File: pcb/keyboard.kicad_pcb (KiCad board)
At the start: 4 copper layers, 141 x 99 mm, 29 parts

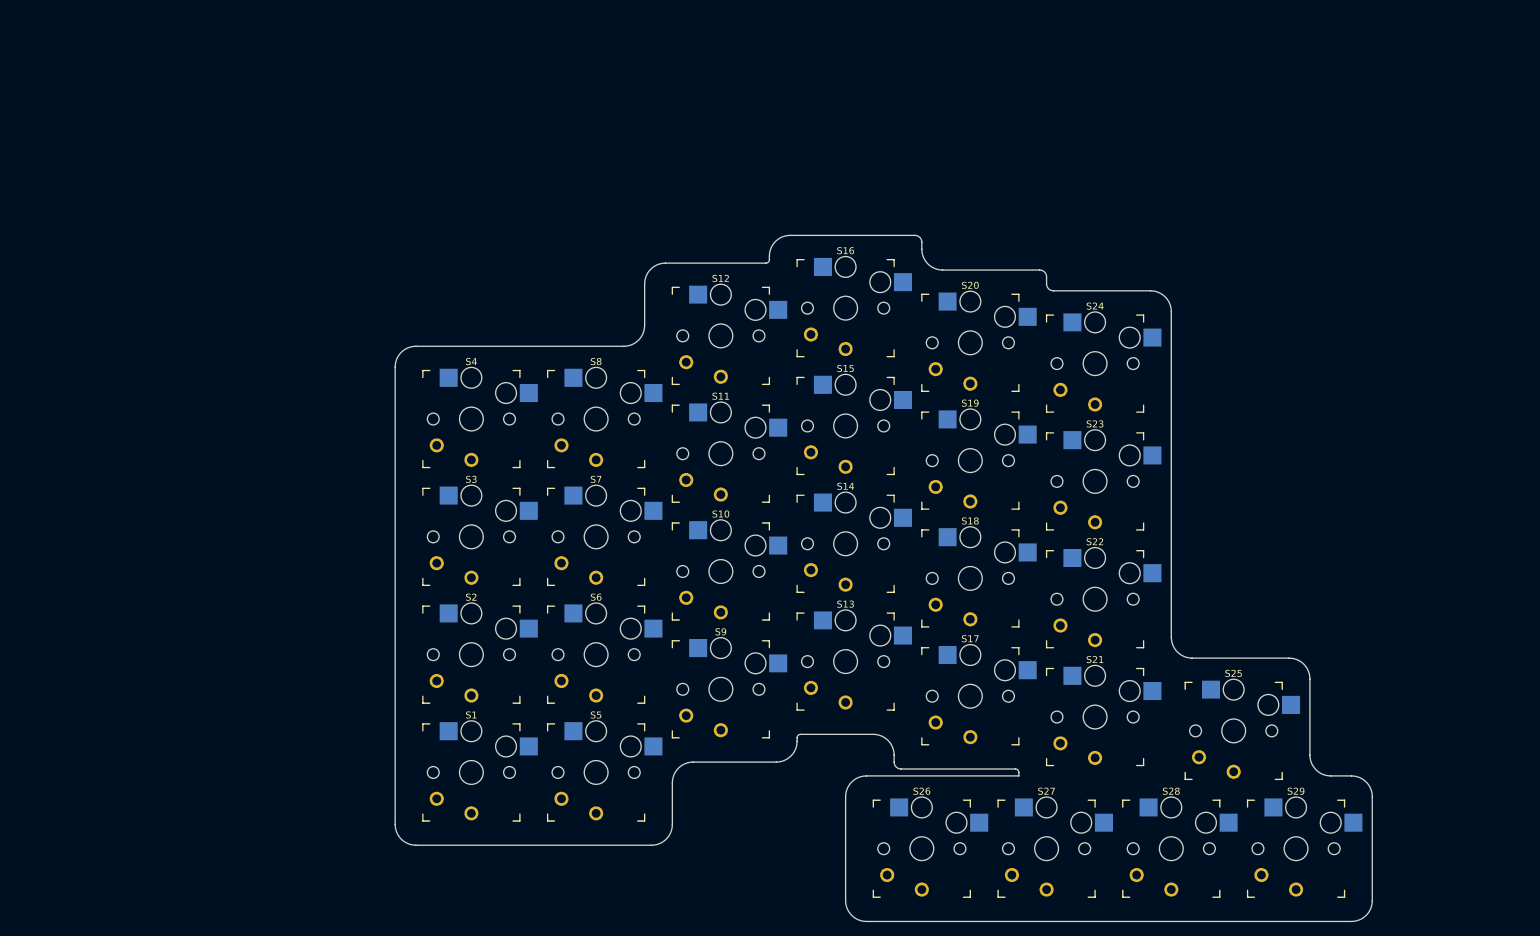
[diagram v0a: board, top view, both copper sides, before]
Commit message: #2 Import schematic components to the PCB
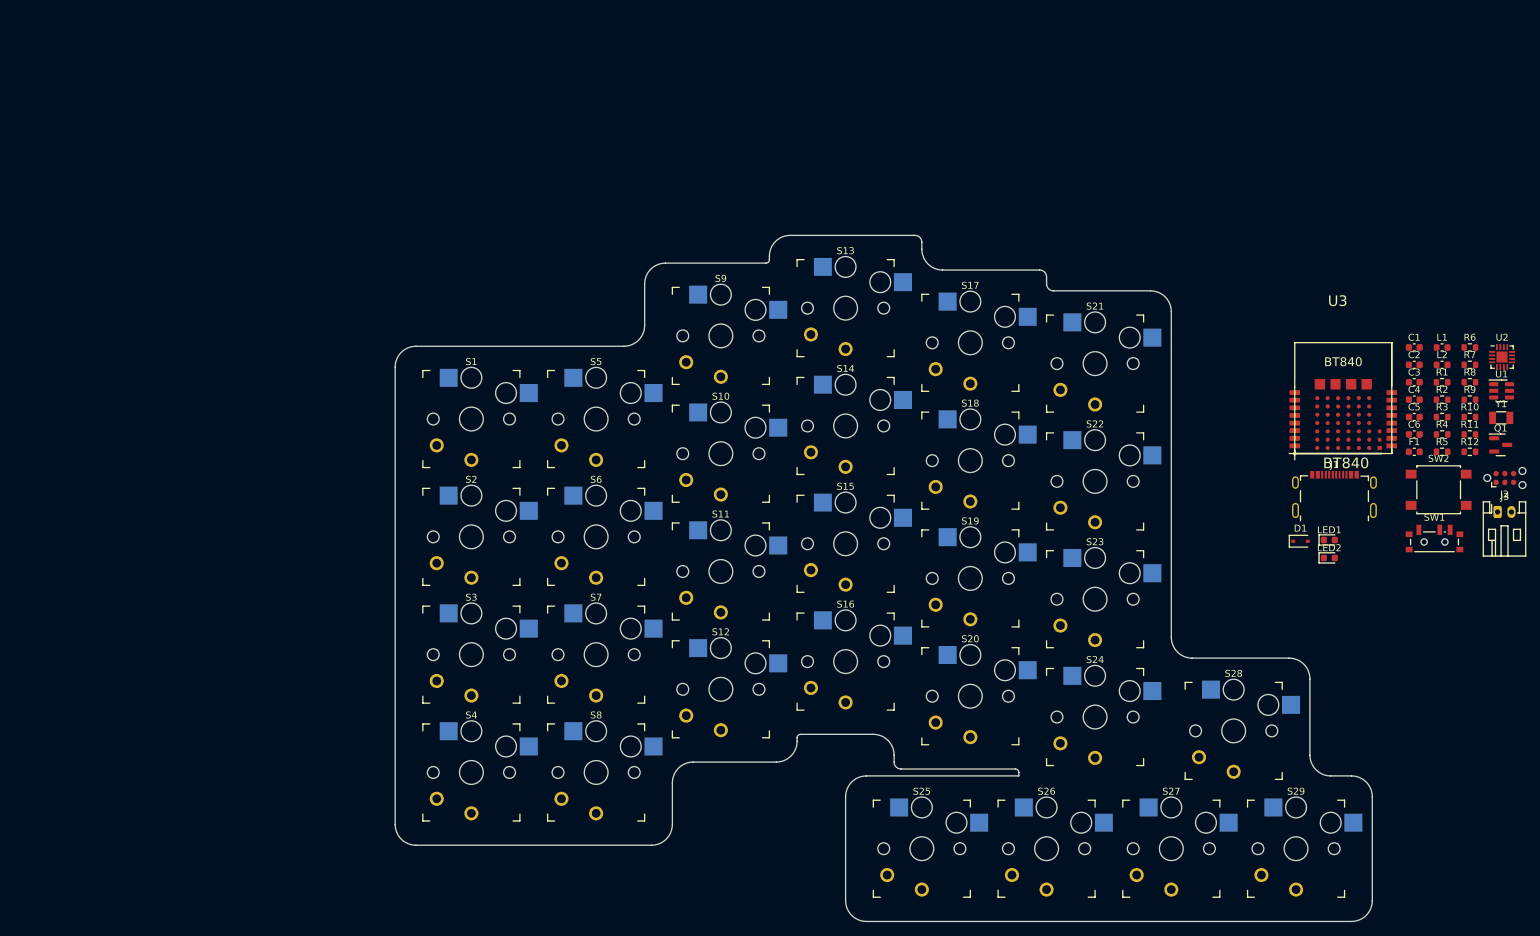
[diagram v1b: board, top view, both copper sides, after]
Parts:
- added C1: 100 nF, Capacitor_SMD:C_0603_1608Metric, F.Cu at (280.2, 88.5)
- added C2: 4.7 uF, Capacitor_SMD:C_0603_1608Metric, F.Cu at (280.2, 91.0)
- added C3: 4.7 uF, Capacitor_SMD:C_0603_1608Metric, F.Cu at (280.2, 93.5)
- added C4: 4.7 uF, Capacitor_SMD:C_0603_1608Metric, F.Cu at (280.2, 96.0)
- added C5: 12pF, Capacitor_SMD:C_0603_1608Metric, F.Cu at (280.2, 98.5)
- added C6: 12pF, Capacitor_SMD:C_0603_1608Metric, F.Cu at (280.2, 101.1)
- added D1: STS321050B100, Diode_SMD:D_SOD-323, F.Cu at (263.8, 116.5)
- added F1: ERB-RE0R75V, Fuse:Fuse_0603_1608Metric, F.Cu at (280.2, 103.6)
- added J1: USB4510-03-1-A, keyboard:USB_C_Receptacle_GCT_USB4510-03-1-A, F.Cu at (268.7, 111.1)
- added J2: Battery, Connector_JST:JST_PH_S2B-PH-K_1x02_P2.00mm_Horizontal, F.Cu at (292.2, 112.2)
- added J3: Tag-Connect TC2030, Connector:Tag-Connect_TC2030-IDC-NL_2x03_P1.27mm_Vertical, F.Cu at (293.2, 107.3)
- added L1: BLM18SG121TN1D, Inductor_SMD:L_0603_1608Metric, F.Cu at (284.2, 88.5)
- added L2: BLM18SG121TN1D, Inductor_SMD:L_0603_1608Metric, F.Cu at (284.2, 91.0)
- added LED1: orange, LED_SMD:LED_0603_1608Metric, F.Cu at (267.9, 116.3)
- added LED2: green, LED_SMD:LED_0603_1608Metric, F.Cu at (267.9, 118.9)
- added Q1: 2N7002, Package_TO_SOT_SMD:SOT-23, F.Cu at (292.6, 102.6)
- added R1: 1 MOhm, Resistor_SMD:R_0603_1608Metric, F.Cu at (284.2, 93.5)
- added R10: 10 kOhm, Resistor_SMD:R_0603_1608Metric, F.Cu at (288.2, 98.5)
- added R11: 100 kOhm, Resistor_SMD:R_0603_1608Metric, F.Cu at (288.2, 101.1)
- added R12: 470 Ohm, Resistor_SMD:R_0603_1608Metric, F.Cu at (288.2, 103.6)
- added R2: 5.1 kOhm, Resistor_SMD:R_0603_1608Metric, F.Cu at (284.2, 96.0)
- added R3: 5.1 kOhm, Resistor_SMD:R_0603_1608Metric, F.Cu at (284.2, 98.5)
- added R4: 47 kOhm, Resistor_SMD:R_0603_1608Metric, F.Cu at (284.2, 101.1)
- added R5: 1.5 kOhm, Resistor_SMD:R_0603_1608Metric, F.Cu at (284.2, 103.6)
- added R6: 5.6 kOhm, Resistor_SMD:R_0603_1608Metric, F.Cu at (288.2, 88.5)
- added R7: 10 kOhm, Resistor_SMD:R_0603_1608Metric, F.Cu at (288.2, 91.0)
- added R8: 1.5 kOhm, Resistor_SMD:R_0603_1608Metric, F.Cu at (288.2, 93.5)
- added R9: 100 Ohm, Resistor_SMD:R_0603_1608Metric, F.Cu at (288.2, 96.0)
- added SW1: PWR, keyboard:SW_SPDT_PCM12, F.Cu at (283.1, 116.2)
- added SW2: Reset, Button_Switch_SMD:SW_SPST_B3S-1000, F.Cu at (283.7, 109.0)
- added U1: SRV05-4, Package_TO_SOT_SMD:SOT-23-6, F.Cu at (292.8, 94.8)
- added U2: BQ24075, Package_DFN_QFN:VQFN-16-1EP_3x3mm_P0.5mm_EP1.6x1.6mm, F.Cu at (292.9, 89.9)
- added U3: BT840, keyboard:Fanstel_BT840, F.Cu at (262.9, 103.8)
- added Y1: ECS-.327-9-34B-TR, Crystal:Crystal_SMD_3215-2Pin_3.2x1.5mm, F.Cu at (292.7, 98.7)
- S1: renamed from S4; footprint kali_choc_v1:Kailh_socket_PG1350_optional -> keyboard:Kailh_socket_PG1350_optional
- S10: renamed from S11; footprint kali_choc_v1:Kailh_socket_PG1350_optional -> keyboard:Kailh_socket_PG1350_optional
- S11: renamed from S10; footprint kali_choc_v1:Kailh_socket_PG1350_optional -> keyboard:Kailh_socket_PG1350_optional
- S12: renamed from S9; footprint kali_choc_v1:Kailh_socket_PG1350_optional -> keyboard:Kailh_socket_PG1350_optional
- S13: renamed from S16; footprint kali_choc_v1:Kailh_socket_PG1350_optional -> keyboard:Kailh_socket_PG1350_optional
- S14: renamed from S15; footprint kali_choc_v1:Kailh_socket_PG1350_optional -> keyboard:Kailh_socket_PG1350_optional
- S15: renamed from S14; footprint kali_choc_v1:Kailh_socket_PG1350_optional -> keyboard:Kailh_socket_PG1350_optional
- S16: renamed from S13; footprint kali_choc_v1:Kailh_socket_PG1350_optional -> keyboard:Kailh_socket_PG1350_optional
- S17: renamed from S20; footprint kali_choc_v1:Kailh_socket_PG1350_optional -> keyboard:Kailh_socket_PG1350_optional
- S18: renamed from S19; footprint kali_choc_v1:Kailh_socket_PG1350_optional -> keyboard:Kailh_socket_PG1350_optional
- S19: renamed from S18; footprint kali_choc_v1:Kailh_socket_PG1350_optional -> keyboard:Kailh_socket_PG1350_optional
- S2: renamed from S3; footprint kali_choc_v1:Kailh_socket_PG1350_optional -> keyboard:Kailh_socket_PG1350_optional
- S20: renamed from S17; footprint kali_choc_v1:Kailh_socket_PG1350_optional -> keyboard:Kailh_socket_PG1350_optional
- S21: renamed from S24; footprint kali_choc_v1:Kailh_socket_PG1350_optional -> keyboard:Kailh_socket_PG1350_optional
- S22: renamed from S23; footprint kali_choc_v1:Kailh_socket_PG1350_optional -> keyboard:Kailh_socket_PG1350_optional
- S23: renamed from S22; footprint kali_choc_v1:Kailh_socket_PG1350_optional -> keyboard:Kailh_socket_PG1350_optional
- S24: renamed from S21; footprint kali_choc_v1:Kailh_socket_PG1350_optional -> keyboard:Kailh_socket_PG1350_optional
- S25: renamed from S26; footprint kali_choc_v1:Kailh_socket_PG1350_optional -> keyboard:Kailh_socket_PG1350_optional
- S26: renamed from S27; footprint kali_choc_v1:Kailh_socket_PG1350_optional -> keyboard:Kailh_socket_PG1350_optional
- S27: renamed from S28; footprint kali_choc_v1:Kailh_socket_PG1350_optional -> keyboard:Kailh_socket_PG1350_optional
- S28: renamed from S25; footprint kali_choc_v1:Kailh_socket_PG1350_optional -> keyboard:Kailh_socket_PG1350_optional
- S29: footprint kali_choc_v1:Kailh_socket_PG1350_optional -> keyboard:Kailh_socket_PG1350_optional
- S3: renamed from S2; footprint kali_choc_v1:Kailh_socket_PG1350_optional -> keyboard:Kailh_socket_PG1350_optional
- S4: renamed from S1; footprint kali_choc_v1:Kailh_socket_PG1350_optional -> keyboard:Kailh_socket_PG1350_optional
- S5: renamed from S8; footprint kali_choc_v1:Kailh_socket_PG1350_optional -> keyboard:Kailh_socket_PG1350_optional
- S6: renamed from S7; footprint kali_choc_v1:Kailh_socket_PG1350_optional -> keyboard:Kailh_socket_PG1350_optional
- S7: renamed from S6; footprint kali_choc_v1:Kailh_socket_PG1350_optional -> keyboard:Kailh_socket_PG1350_optional
- S8: renamed from S5; footprint kali_choc_v1:Kailh_socket_PG1350_optional -> keyboard:Kailh_socket_PG1350_optional
- S9: renamed from S12; footprint kali_choc_v1:Kailh_socket_PG1350_optional -> keyboard:Kailh_socket_PG1350_optional
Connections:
- net /GND renamed GND
- S1 pad 1: /P3 -> P0.26
- S10 pad 1: /P10 -> P0.29
- S11 pad 1: /P9 -> P1.10
- S12 pad 1: /P8 -> P1.08
- S13 pad 1: /P15 -> P0.28
- S14 pad 1: /P14 -> P1.14
- S15 pad 1: /P13 -> P0.07
- S16 pad 1: /P12 -> P1.03
- S17 pad 1: /P19 -> P0.24
- S18 pad 1: /P18 -> P0.04
- S19 pad 1: /P17 -> P0.08
- S2 pad 1: /P2 -> P0.27
- S20 pad 1: /P16 -> P1.04
- S21 pad 1: /P23 -> P0.23
- S22 pad 1: /P22 -> P0.20
- S23 pad 1: /P21 -> P1.02
- S24 pad 1: /P20 -> P1.05
- S25 pad 1: /P25 -> P0.12
- S26 pad 1: /P26 -> P0.25
- S27 pad 1: /P27 -> P1.07
- S28 pad 1: /P24 -> P0.21
- S29 pad 1: /P28 -> P0.21
- S3 pad 1: /P1 -> unconnected-(S3-Pad1)
- S4 pad 1: /P0 -> unconnected-(S4-Pad1)
- S5 pad 1: /P7 -> P1.11
- S6 pad 1: /P6 -> P1.12
- S7 pad 1: /P5 -> P0.05
- S8 pad 1: /P4 -> P1.06
- S9 pad 1: /P11 -> P1.13

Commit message: #2 add JLCPCB design rules
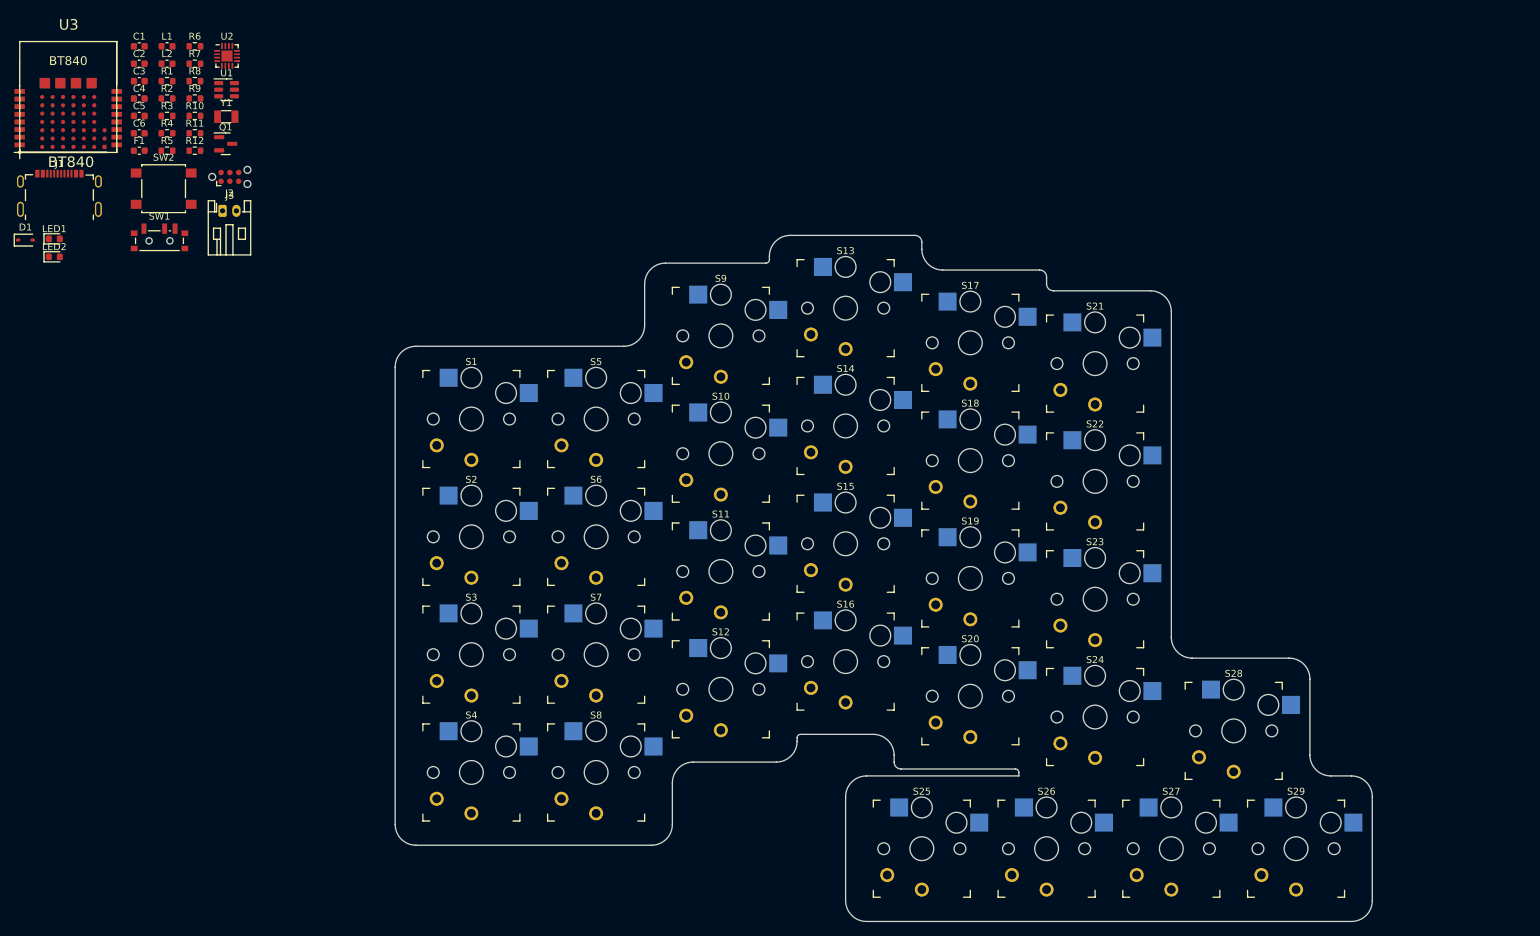
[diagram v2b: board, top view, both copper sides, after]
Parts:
- moved C1 189.0 mm to (96.2, 45.1)
- moved C2 189.0 mm to (96.2, 47.6)
- moved C3 189.0 mm to (96.2, 50.1)
- moved C4 189.0 mm to (96.2, 52.6)
- moved C5 189.0 mm to (96.2, 55.1)
- moved C6 189.0 mm to (96.2, 57.6)
- moved D1 189.0 mm to (79.8, 73.0)
- moved F1 189.0 mm to (96.2, 60.1)
- moved J1 189.0 mm to (84.7, 67.6)
- moved J3 189.0 mm to (109.3, 63.9)
- moved L1 189.0 mm to (100.2, 45.1)
- moved L2 189.0 mm to (100.2, 47.6)
- moved LED1 189.0 mm to (83.9, 72.8)
- moved LED2 189.0 mm to (83.9, 75.4)
- moved R1 189.0 mm to (100.2, 50.1)
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
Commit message: #2 add pcb outline,roughly place components
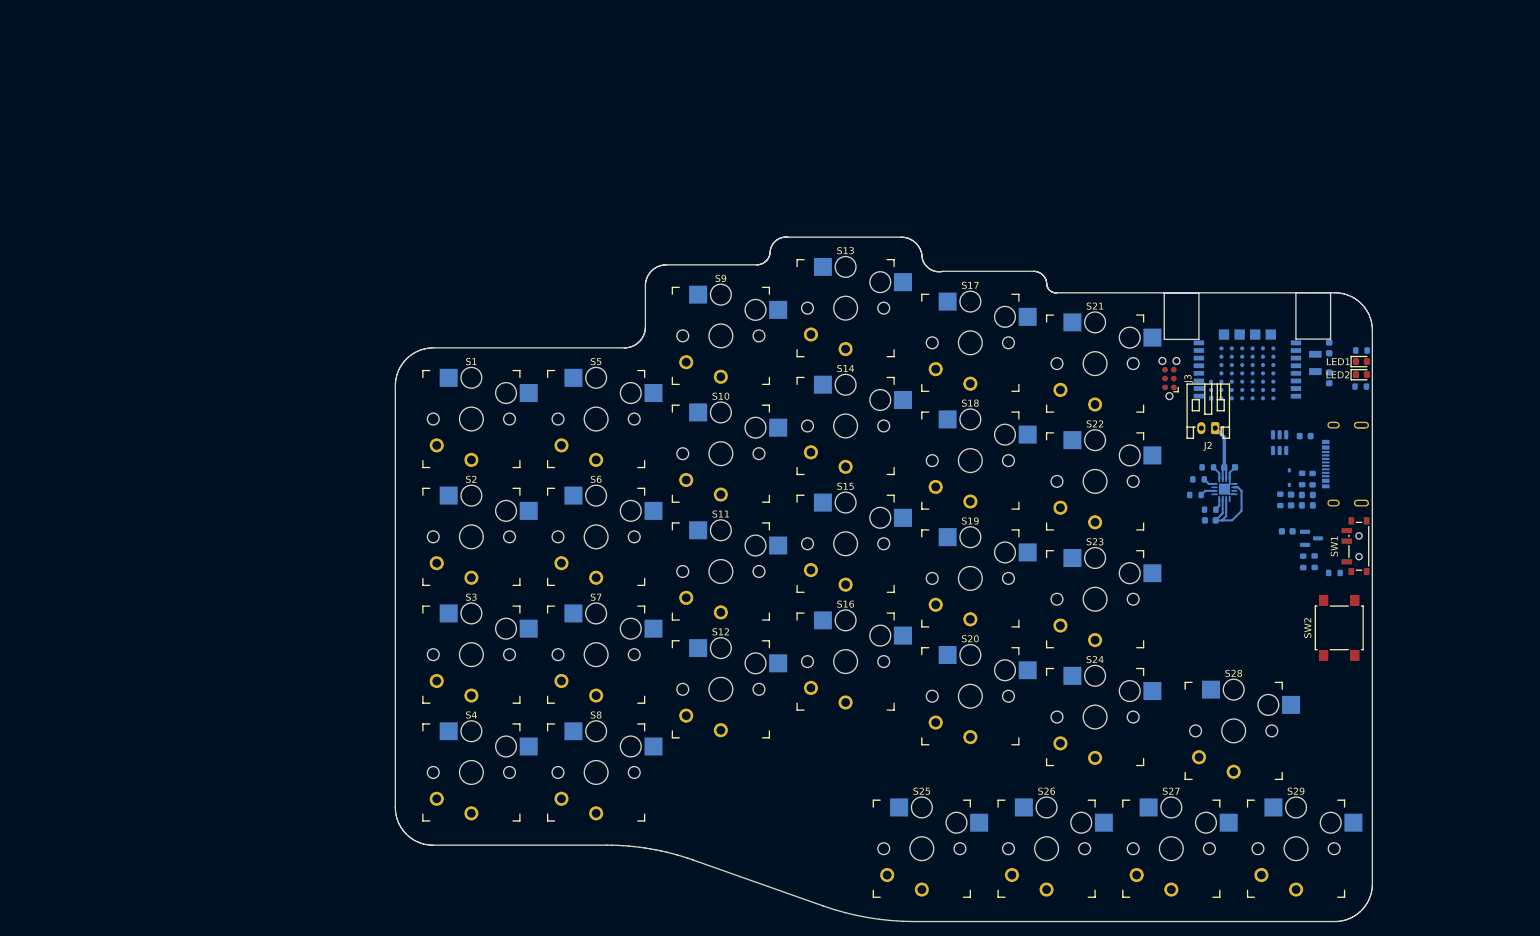
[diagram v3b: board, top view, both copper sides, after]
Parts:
- C1, C2, C3, C4, C5, C6, D1, F1, J1, L1, L2, Q1, R1, R10, R11, R12, R2, R3, R4, R5, R6, R7, R8, R9, U1, U2, U3, Y1: moved to B.Cu
- moved J1 190.7 mm to (271.6, 105.3), turned to -90 degrees
- moved LED1 189.4 mm to (272.6, 90.5)
- moved LED2 189.4 mm to (272.6, 92.5)
- moved U3 187.7 mm to (263.1, 96.6), turned to 180 degrees
- moved D1 185.6 mm to (262.1, 107.3), turned to 90 degrees
- moved SW2 181.1 mm to (269.4, 129.0), turned to 90 degrees
- moved C2 178.9 mm to (261.9, 115.0)
- moved C1 178.6 mm to (262.4, 110.5), turned to -90 degrees
- moved SW1 178.4 mm to (271.9, 117.2), turned to 90 degrees
- moved R11 176.3 mm to (268.6, 121.0), turned to 180 degrees
- moved F1 176.2 mm to (264.8, 111.3)
- moved L2 175.9 mm to (264.8, 109.8), turned to 180 degrees
- moved C6 175.3 mm to (267.9, 92.9), turned to 90 degrees
- moved C5 174.9 mm to (267.9, 88.6), turned to -90 degrees
- moved R9 174.9 mm to (265.8, 119.4), turned to -90 degrees
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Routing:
- net +VSW: track 0.00 -> 15.3 mm
- net +BATT: track 0.00 -> 9.81 mm
- net GND: track 0.00 -> 6.20 mm
- net Net-(U2-TMR): track 0.00 -> 2.17 mm
- net Net-(U2-TS): track 0.00 -> 2.04 mm
- net Net-(U2-ISET): track 0.00 -> 1.75 mm
- net Net-(U2-ILIM): track 0.00 -> 1.72 mm
- added copper zone on In1.Cu, net GND
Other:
- board size 141 x 99 mm -> 141 x 98.8 mm
